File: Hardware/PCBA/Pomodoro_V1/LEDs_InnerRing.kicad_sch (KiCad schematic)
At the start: 0 parts

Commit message: Updated CubeMx File, Created Schematic for µC, layouted the LEDs on the PCB
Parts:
- added C13: 1u, symbol Device:C
- added C15: 100n, symbol Device:C
- added D101, D103, D105, D107, D109, D111, D113, D115, D117, D119, D91, D93, D95, D97, D99: WS2812B-2020, LED_SMD:LED_WS2812B-2020_PLCC4_2.0x2.0mm, symbol LED:WS2812B-2020
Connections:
- new net: D97.1 (DOUT), D99.3 (DIN)
- new net: D95.1 (DOUT), D97.3 (DIN)
- new net: D101.1 (DOUT), D103.3 (DIN)
- new net: D101.3 (DIN), D99.1 (DOUT)
- new net: D105.1 (DOUT), D107.3 (DIN)
- new net: D103.1 (DOUT), D105.3 (DIN)
- new net: D111.1 (DOUT), D113.3 (DIN)
- new net: D109.1 (DOUT), D111.3 (DIN)
- new net: D107.1 (DOUT), D109.3 (DIN)
- new net: D113.1 (DOUT), D115.3 (DIN)
- new net: D115.1 (DOUT), D117.3 (DIN)
- new net: D93.1 (DOUT), D95.3 (DIN)
- new net: D91.1 (DOUT), D93.3 (DIN)
- new net: D117.1 (DOUT), D119.3 (DIN)
- new net +5V: C13.1, C15.1, D101.4 (VDD), D103.4 (VDD), D105.4 (VDD), D107.4 (VDD), D109.4 (VDD), D111.4 (VDD), D113.4 (VDD), D115.4 (VDD), D117.4 (VDD), D119.4 (VDD), D91.4 (VDD), D93.4 (VDD), D95.4 (VDD), D97.4 (VDD), D99.4 (VDD)
- new net GND: C13.2, C15.2, D101.2 (VSS), D103.2 (VSS), D105.2 (VSS), D107.2 (VSS), D109.2 (VSS), D111.2 (VSS), D113.2 (VSS), D115.2 (VSS), D117.2 (VSS), D119.2 (VSS), D91.2 (VSS), D93.2 (VSS), D95.2 (VSS), D97.2 (VSS), D99.2 (VSS)
- new net TIM1_CH1 (RgbLed Inner Ring): D91.3 (DIN)

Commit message: added the accelerometer to the Schematic
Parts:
- renumbered C15 to C14, D109 to D100, D111 to D101, D113 to D102, D115 to D103, D117 to D104, D119 to D105, D93 to D92, D95 to D93, D97 to D94, D99 to D95, D101 to D96, D103 to D97, D105 to D98, D107 to D99
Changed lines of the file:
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@@
 		(on_board yes)
 		(dnp no)
-		(property "Reference" "D97"
+		(property "Reference" "D94"
 			(at 99.314 40.64 0)
 			(effects
@@
 			(project "Pomodoro_V1"
 				(path "/8b8515f0-2a7a-4fc4-bc5a-86877c499298/229321d6-581c-43f0-99a7-d20c362b1348/e017012d-e48e-4e14-a006-0fecebf06543"
-					(reference "D97")
+					(reference "D94")
 					(unit 1)
 				)
@@
 		(on_board yes)
 		(dnp no)
-		(property "Reference" "D101"
+		(property "Reference" "D96"
 			(at 129.794 40.64 0)
 			(effects
@@
 			(project "Pomodoro_V1"
 				(path "/8b8515f0-2a7a-4fc4-bc5a-86877c499298/229321d6-581c-43f0-99a7-d20c362b1348/e017012d-e48e-4e14-a006-0fecebf06543"
-					(reference "D101")
+					(reference "D96")
 					(unit 1)
 				)
@@
 		(dnp no)
 		(fields_autoplaced yes)
-		(property "Reference" "C15"
+		(property "Reference" "C14"
 			(at 63.5 81.2799 0)
 			(effects
@@
 			(project "Pomodoro_V1"
 				(path "/8b8515f0-2a7a-4fc4-bc5a-86877c499298/229321d6-581c-43f0-99a7-d20c362b1348/e017012d-e48e-4e14-a006-0fecebf06543"
-					(reference "C15")
+					(reference "C14")
 					(unit 1)
 				)
@@
 		(on_board yes)
 		(dnp no)
-		(property "Reference" "D105"
+		(property "Reference" "D98"
 			(at 160.274 40.64 0)
 			(effects
@@
 			(project "Pomodoro_V1"
 				(path "/8b8515f0-2a7a-4fc4-bc5a-86877c499298/229321d6-581c-43f0-99a7-d20c362b1348/e017012d-e48e-4e14-a006-0fecebf06543"
-					(reference "D105")
+					(reference "D98")
 					(unit 1)
 				)
@@
 		(on_board yes)
 		(dnp no)
-		(property "Reference" "D111"
+		(property "Reference" "D101"
 			(at 205.994 40.64 0)
 			(effects
@@
 			(project "Pomodoro_V1"
 				(path "/8b8515f0-2a7a-4fc4-bc5a-86877c499298/229321d6-581c-43f0-99a7-d20c362b1348/e017012d-e48e-4e14-a006-0fecebf06543"
-					(reference "D111")
+					(reference "D101")
 					(unit 1)
 				)
@@
 		(dnp no)
 		(fields_autoplaced yes)
-		(property "Reference" "#PWR029"
+		(property "Reference" "#PWR025"
 			(at 49.53 43.18 0)
 			(effects
@@
 			(project "Pomodoro_V1"
 				(path "/8b8515f0-2a7a-4fc4-bc5a-86877c499298/229321d6-581c-43f0-99a7-d20c362b1348/e017012d-e48e-4e14-a006-0fecebf06543"
-					(reference "#PWR029")
+					(reference "#PWR025")
 					(unit 1)
 				)
@@
 		(on_board yes)
 		(dnp no)
-		(property "Reference" "D99"
+		(property "Reference" "D95"
 			(at 114.554 40.64 0)
 			(effects
@@
 			(project "Pomodoro_V1"
 				(path "/8b8515f0-2a7a-4fc4-bc5a-86877c499298/229321d6-581c-43f0-99a7-d20c362b1348/e017012d-e48e-4e14-a006-0fecebf06543"
-					(reference "D99")
+					(reference "D95")
 					(unit 1)
 				)
@@
 		(on_board yes)
 		(dnp no)
-		(property "Reference" "D103"
+		(property "Reference" "D97"
 			(at 145.034 40.64 0)
 			(effects
@@
 			(project "Pomodoro_V1"
 				(path "/8b8515f0-2a7a-4fc4-bc5a-86877c499298/229321d6-581c-43f0-99a7-d20c362b1348/e017012d-e48e-4e14-a006-0fecebf06543"
-					(reference "D103")
+					(reference "D97")
 					(unit 1)
 				)
@@
 		(on_board yes)
 		(dnp no)
-		(property "Reference" "D109"
+		(property "Reference" "D100"
 			(at 190.754 40.64 0)
 			(effects
@@
 			(project "Pomodoro_V1"
 				(path "/8b8515f0-2a7a-4fc4-bc5a-86877c499298/229321d6-581c-43f0-99a7-d20c362b1348/e017012d-e48e-4e14-a006-0fecebf06543"
-					(reference "D109")
+					(reference "D100")
 					(unit 1)
 				)
@@
 		(dnp no)
 		(fields_autoplaced yes)
-		(property "Reference" "#PWR030"
+		(property "Reference" "#PWR026"
 			(at 49.53 60.96 0)
 			(effects
@@
 			(project "Pomodoro_V1"
 				(path "/8b8515f0-2a7a-4fc4-bc5a-86877c499298/229321d6-581c-43f0-99a7-d20c362b1348/e017012d-e48e-4e14-a006-0fecebf06543"
-					(reference "#PWR030")
+					(reference "#PWR026")
 					(unit 1)
 				)
@@
 		(on_board yes)
 		(dnp no)
-		(property "Reference" "D113"
+		(property "Reference" "D102"
 			(at 221.234 40.64 0)
 			(effects
@@
 			(project "Pomodoro_V1"
 				(path "/8b8515f0-2a7a-4fc4-bc5a-86877c499298/229321d6-581c-43f0-99a7-d20c362b1348/e017012d-e48e-4e14-a006-0fecebf06543"
-					(reference "D113")
+					(reference "D102")
 					(unit 1)
 				)
@@
 		(on_board yes)
 		(dnp no)
-		(property "Reference" "D107"
+		(property "Reference" "D99"
 			(at 175.514 40.64 0)
 			(effects
@@
 			(project "Pomodoro_V1"
 				(path "/8b8515f0-2a7a-4fc4-bc5a-86877c499298/229321d6-581c-43f0-99a7-d20c362b1348/e017012d-e48e-4e14-a006-0fecebf06543"
-					(reference "D107")
+					(reference "D99")
 					(unit 1)
 				)
@@
 		(on_board yes)
 		(dnp no)
-		(property "Reference" "D115"
+		(property "Reference" "D103"
 			(at 236.474 40.64 0)
 			(effects
@@
 			(project "Pomodoro_V1"
 				(path "/8b8515f0-2a7a-4fc4-bc5a-86877c499298/229321d6-581c-43f0-99a7-d20c362b1348/e017012d-e48e-4e14-a006-0fecebf06543"
-					(reference "D115")
+					(reference "D103")
 					(unit 1)
 				)
@@
 		(on_board yes)
 		(dnp no)
-		(property "Reference" "D93"
+		(property "Reference" "D92"
 			(at 68.834 40.64 0)
 			(effects
@@
 			(project "Pomodoro_V1"
 				(path "/8b8515f0-2a7a-4fc4-bc5a-86877c499298/229321d6-581c-43f0-99a7-d20c362b1348/e017012d-e48e-4e14-a006-0fecebf06543"
-					(reference "D93")
+					(reference "D92")
 					(unit 1)
 				)
@@
 		(dnp no)
 		(fields_autoplaced yes)
-		(property "Reference" "#PWR026"
+		(property "Reference" "#PWR030"
 			(at 49.53 96.52 0)
 			(effects
@@
 			(project "Pomodoro_V1"
 				(path "/8b8515f0-2a7a-4fc4-bc5a-86877c499298/229321d6-581c-43f0-99a7-d20c362b1348/e017012d-e48e-4e14-a006-0fecebf06543"
-					(reference "#PWR026")
+					(reference "#PWR030")
 					(unit 1)
 				)
@@
 		(on_board yes)
 		(dnp no)
-		(property "Reference" "D117"
+		(property "Reference" "D104"
 			(at 251.714 40.64 0)
 			(effects
@@
 			(project "Pomodoro_V1"
 				(path "/8b8515f0-2a7a-4fc4-bc5a-86877c499298/229321d6-581c-43f0-99a7-d20c362b1348/e017012d-e48e-4e14-a006-0fecebf06543"
-					(reference "D117")
+					(reference "D104")
 					(unit 1)
 				)
@@
 		(on_board yes)
 		(dnp no)
-		(property "Reference" "D119"
+		(property "Reference" "D105"
 			(at 266.954 40.64 0)
 			(effects
@@
 			(project "Pomodoro_V1"
 				(path "/8b8515f0-2a7a-4fc4-bc5a-86877c499298/229321d6-581c-43f0-99a7-d20c362b1348/e017012d-e48e-4e14-a006-0fecebf06543"
-					(reference "D119")
+					(reference "D105")
 					(unit 1)
 				)
@@
 		(on_board yes)
 		(dnp no)
-		(property "Reference" "D95"
+		(property "Reference" "D93"
 			(at 84.074 40.64 0)
 			(effects
@@
 			(project "Pomodoro_V1"
 				(path "/8b8515f0-2a7a-4fc4-bc5a-86877c499298/229321d6-581c-43f0-99a7-d20c362b1348/e017012d-e48e-4e14-a006-0fecebf06543"
-					(reference "D95")
+					(reference "D93")
 					(unit 1)
 				)
@@
 		(dnp no)
 		(fields_autoplaced yes)
-		(property "Reference" "#PWR025"
+		(property "Reference" "#PWR029"
 			(at 49.53 78.74 0)
 			(effects
@@
 			(project "Pomodoro_V1"
 				(path "/8b8515f0-2a7a-4fc4-bc5a-86877c499298/229321d6-581c-43f0-99a7-d20c362b1348/e017012d-e48e-4e14-a006-0fecebf06543"
-					(reference "#PWR025")
-					(unit 1)
-				)
+					(reference "#PWR029")
+					(unit 1)
+				)

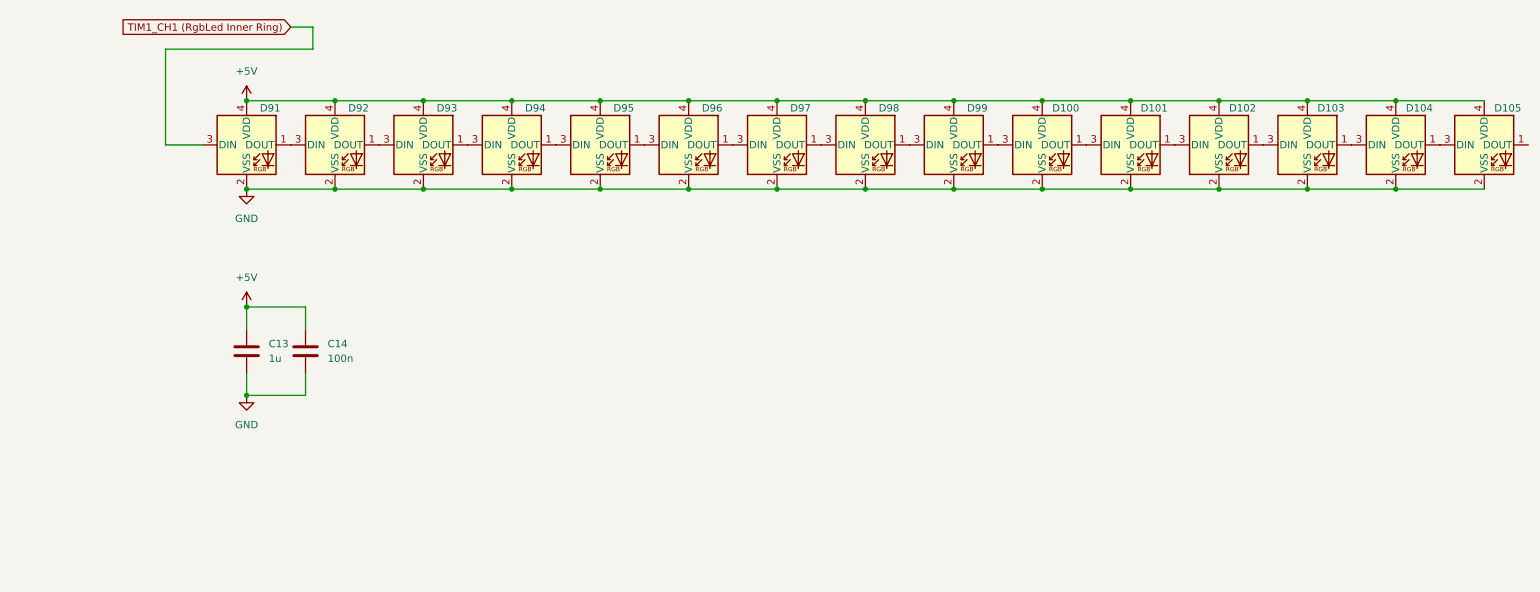
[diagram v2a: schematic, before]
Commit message: Implemented the Rotary encoder, the buttons, the IMU, Added it to the PCB (All the space constraining elements are now placed)
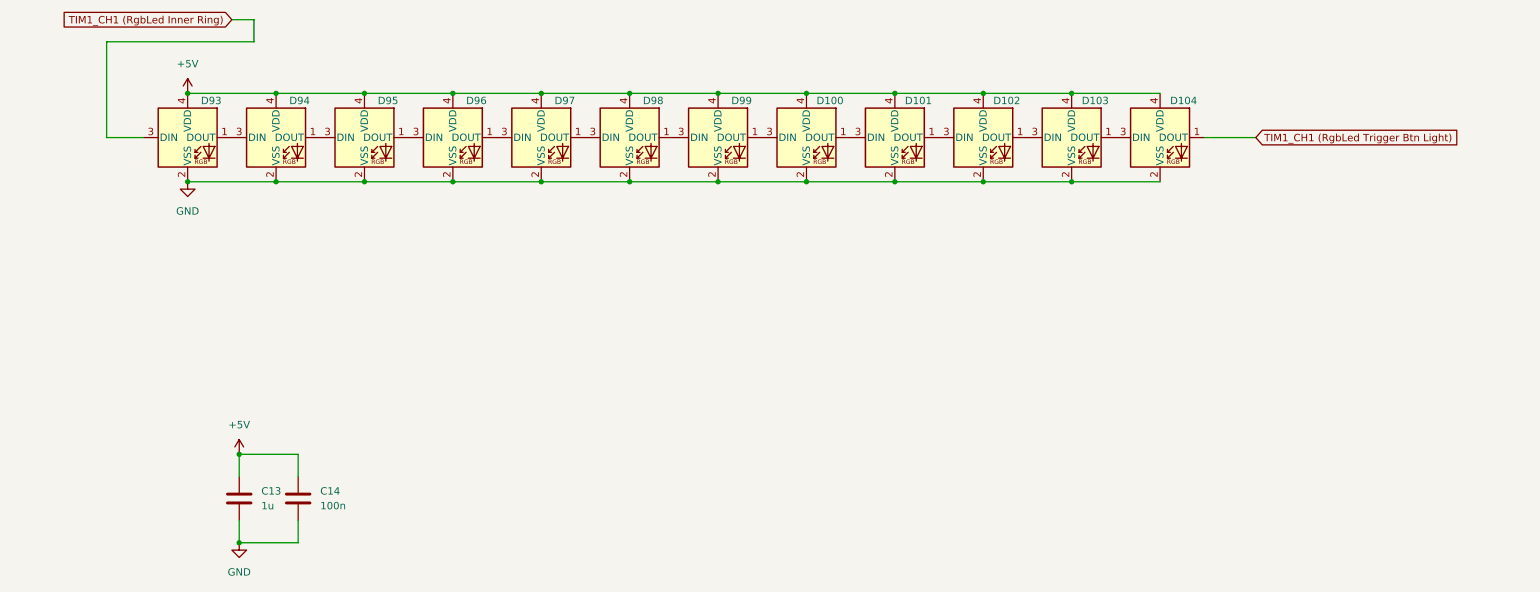
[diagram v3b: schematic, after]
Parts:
- removed D103, D104, D105: WS2812B-2020, LED_SMD:LED_WS2812B-2020_PLCC4_2.0x2.0mm, symbol LED:WS2812B-2020
- renumbered D98 to D100, D99 to D101, D100 to D102, D101 to D103, D102 to D104, D91 to D93, D92 to D94, D93 to D95, D94 to D96, D95 to D97, D96 to D98, D97 to D99
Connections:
- net TIM1_CH1 (RgbLed Trigger Btn Light): now reaches D104.1 (DOUT)
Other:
- moved on the sheet: C13, C14, D100, D101, D102, D103, D104, D93, D94, D95, D96, D97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

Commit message: Finalized the schematic, First Draft of the finished Layout
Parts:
- removed C13: 1u, symbol Device:C
- removed C14: 100n, symbol Device:C

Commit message: Version that was ordered online
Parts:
- D100, D101, D102, D103, D104, D93, D94, D95, D96, D97, D98, D99: MPN (none) -> WS2812B-2020
